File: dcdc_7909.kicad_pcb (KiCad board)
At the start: 4 copper layers, 41.5 x 27 mm, 64 parts, among them J1 V_IN, J2 G_IN, J3 +10V, J4 G_OUT, J5 -10V, J6 Conn_01x01, J7 Conn_01x01, J8 Conn_01x01, J9 Conn_01x01, U1 LM2940-SOT223-15, U2 MAXM15068AMB+, U3 MAX17579ATC+, U4 LT3045xMSE, U5 LT3094xMSE

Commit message: Sent for production.
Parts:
- C12, C5: footprint Capacitor_SMD:C_0805_2012Metric -> Capacitor_SMD:C_1206_3216Metric
- R3: value 1M07 1% -> 499k 1%
- R4: value 150k 1% -> 47k 1%
- R8: value 1M07 1% -> 19k1 1%
- R9: value 150k 1% -> 1k78 1%
- moved C11 4.99 mm to (106.3, 65.1), turned to 180 degrees
- moved C12 2.33 mm to (105.6, 67.8), turned to 180 degrees
- moved R7 2.23 mm to (106.3, 66.0), turned to 0 degrees
- moved C5 0.59 mm to (106.9, 62.6)
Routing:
- net /SS: track 2.94 -> 9.26 mm
- net Net-(C11-Pad2): track 21.4 -> 15.1 mm
- net /RT: track 1.73 -> 4.46 mm
- net GND: vias 167 -> 168

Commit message: Doing calcs + removing caps that might introduce noise.
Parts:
- removed the C17 at (86.6, 56.9)
- removed the C22 at (85.4, 67.6)
- removed the D1 at (115.6, 66.5)
- removed FB1, FB2: 600Ω@100MHz, Resistor_SMD:R_0805_2012Metric
- added C10: C_Polarized_Small, Capacitor_SMD:CP_Elec_6.3x5.9, F.Cu at (115.7, 67.1)
- added L1: 10u, Inductor_SMD:L_0805_2012Metric, F.Cu at (95.8, 61.6)
- added L3: 10u, Inductor_SMD:L_0805_2012Metric, F.Cu at (97.1, 69.3)
- R12: renamed from R11; value 1k -> 6k8
- R13: value 1k -> 6k8
- moved C23 5.64 mm to (85.8, 65.5), turned to -90 degrees
- moved C24 3.31 mm to (83.2, 78.6), turned to -90 degrees
- moved C9 2.69 mm to (112.9, 68.2), turned to 90 degrees
- moved C22 1.29 mm to (83.4, 65.0), turned to -90 degrees
- moved R12 1.26 mm to (87.9, 63.1), turned to -90 degrees
- moved NT3 1.17 mm to (83.8, 76.3), turned to 0 degrees
- moved C21 0.74 mm to (85.4, 77.8), turned to -90 degrees
- moved C25 0.15 mm to (85.4, 73.2)
- renumbered C3 to C1, C6 to C11, C7 to C12, C8 to C14, C14 to C15, C15 to C16, C23 to C17, C16 to C19, C9 to C2, C19 to C20, C24 to C21, C20 to C22, C21 to C23, C25 to C24, C26 to C25, C1 to C3, C10 to C5, C5 to C6, C11 to C7, C12 to C8, C2 to C9, D2 to D1, D3 to D2, J6 to J3, J7 to J4, J8 to J5, J9 to J6, J3 to J7, J4 to J8, J5 to J9, L1 to L2, R12 to R10, R10 to R11, R5 to R3, R6 to R4, R7 to R5, R3 to R6, R4 to R7, U3 to U2, U2 to U3
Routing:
- net /-10V: track 2.96 -> 6.98 mm, vias 4 -> 0
- net VCC: track 1.06 -> 3.91 mm
- net Net-(D1-Pad2): track 17.4 -> 18.9 mm
- net GND: vias 168 -> 171
- removed copper zone on B.Cu, net /-10V

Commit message: Before restructuring max17579.
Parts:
- added R9: 27k 1%, Resistor_SMD:R_0402_1005Metric, F.Cu at (123.7, 65.0)
- L2: footprint Inductor_SMD:L_Coilcraft_XAL60xx_6.36x6.56mm -> marcin_library:Wurth 74408063680
- R10: renamed from R9; value 1k78 1% -> 39k
- R8: value 19k1 1% -> 390k 1%
- renumbered R10 to R11, R11 to R12, R12 to R13, R13 to R14
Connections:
- net Net-(C7-Pad2) renamed /SOUT
- R8 pad 1: /FB_NEG -> Net-(R8-Pad1)

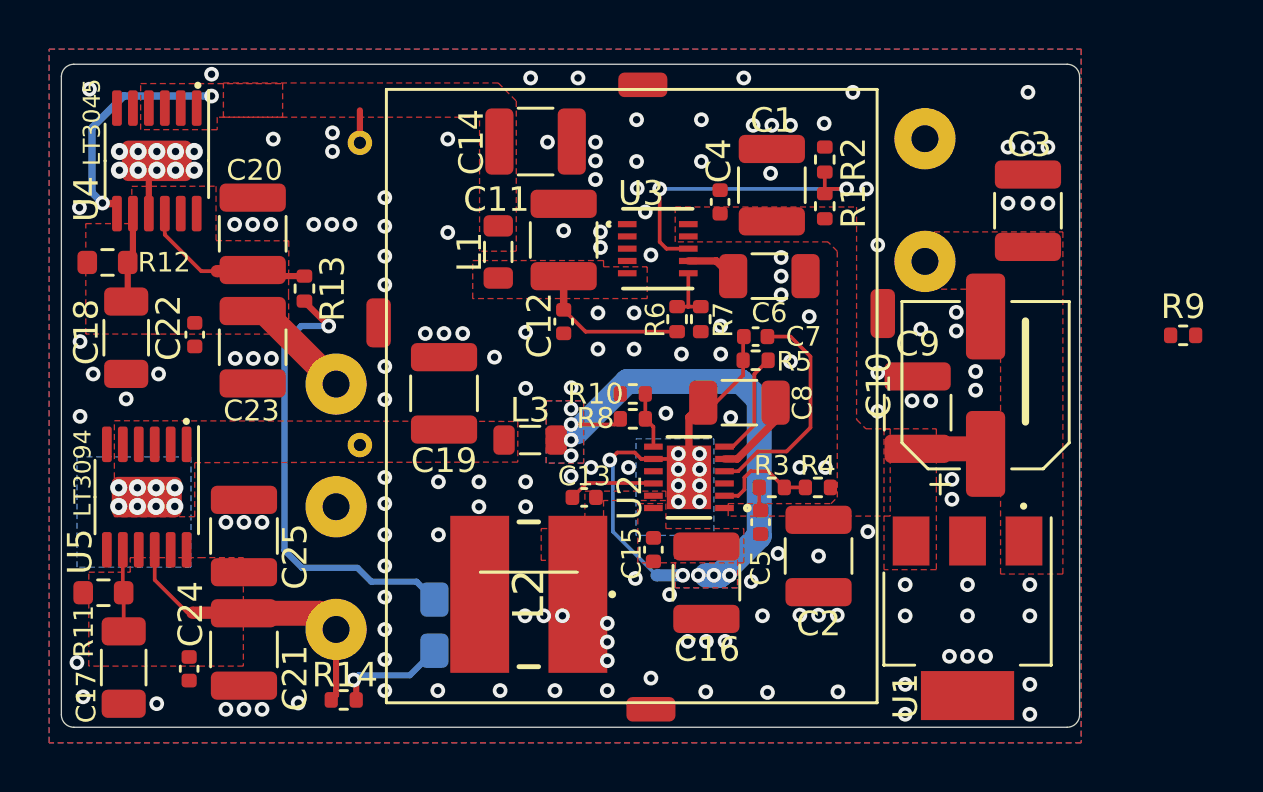
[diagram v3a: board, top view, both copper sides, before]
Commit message: Fix footprints of MAX and MAXM.
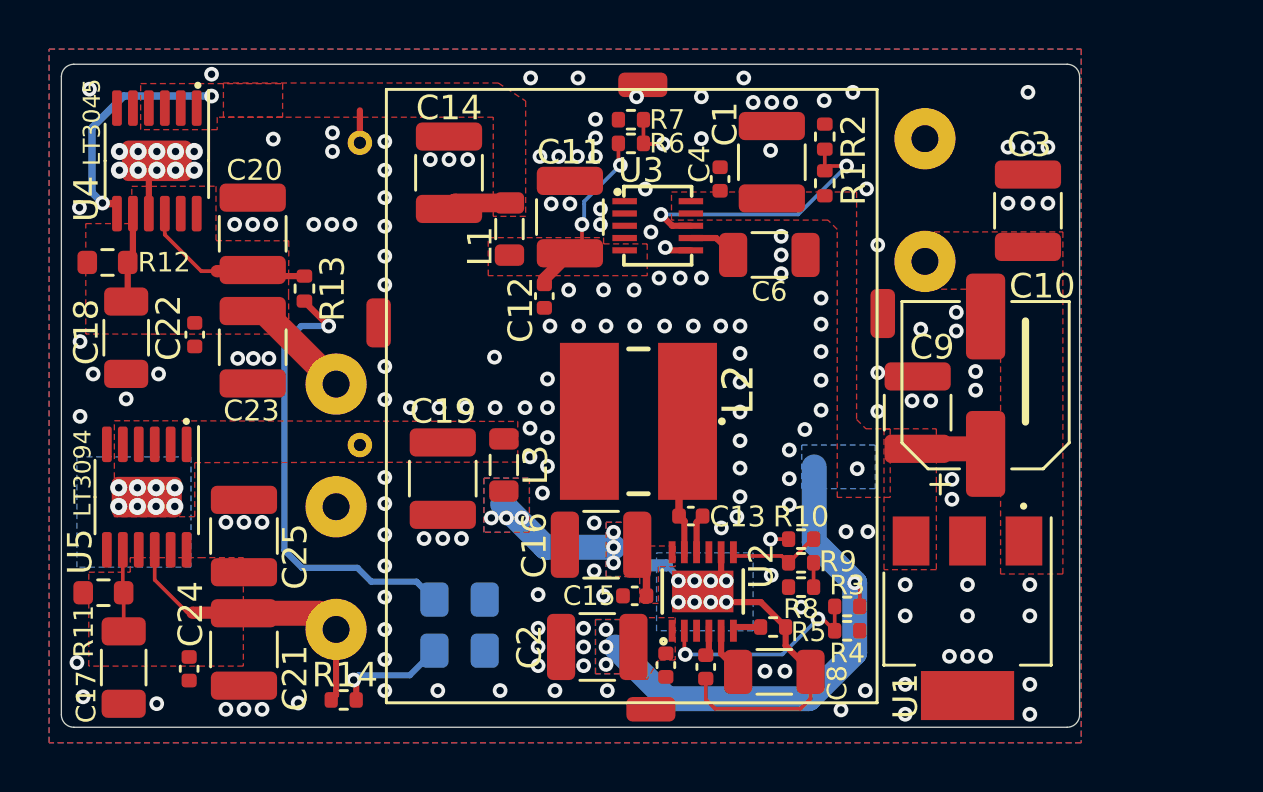
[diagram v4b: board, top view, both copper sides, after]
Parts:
- moved R9 18.1 mm to (108.2, 74.3)
- moved C7 13.6 mm to (104.3, 78.5), turned to -90 degrees
- moved C8 11.1 mm to (107.1, 78.7), turned to 0 degrees
- moved R5 10.9 mm to (107.0, 76.9), turned to 180 degrees
- moved R8 10.4 mm to (108.2, 75.3)
- moved C2 9.75 mm to (99.8, 77.7), turned to 180 degrees
- moved R7 8.61 mm to (101.2, 56.2), turned to 0 degrees
- moved R10 8.43 mm to (108.2, 73.3)
- moved L2 8.35 mm to (101.5, 68.5)
- moved R6 7.41 mm to (101.2, 57.2), turned to 180 degrees
- moved C5 6.99 mm to (102.6, 78.5)
- moved R4 5.96 mm to (110.0, 77.1)
- moved R3 5.74 mm to (110.0, 76.1), turned to 0 degrees
- moved U2 4.69 mm to (104.1, 75.5), turned to 90 degrees
- moved C16 4.56 mm to (100.0, 73.6), turned to 0 degrees
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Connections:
- L2 pad 1: GND -> /LX
- L2 pad 2: /LX -> GND
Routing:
- net VCC: track 3.91 -> 23.6 mm, vias 0 -> 5
- net /FB_POS: track 2.33 -> 10.7 mm, vias 0 -> 2
- net /SS: track 9.26 -> 1.20 mm
- net /LX: track 0.00 -> 5.72 mm
- net /UVLO_NEG: track 4.28 -> 9.02 mm, vias 0 -> 2
- net Net-(C15-Pad2): track 19.1 -> 23.3 mm, vias 8 -> 7
- net /RT: track 4.46 -> 1.11 mm
- net /+10.5: track 10.7 -> 13.2 mm
- net /BST: track 3.55 -> 1.73 mm
- net /SOUT: track 15.1 -> 13.5 mm, vias 9 -> 8
- net /FB_NEG: track 2.29 -> 3.79 mm
- net Net-(C8-Pad1): track 3.46 -> 2.06 mm
- net /UVLO: track 12.9 -> 11.7 mm
- net Net-(R8-Pad1): track 0.00 -> 0.99 mm
- net /OUT_POS: track 6.36 -> 7.06 mm, vias 0 -> 2
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- added copper zone on B.Cu, net VCC
- removed copper zone on F.Cu, net /LX
